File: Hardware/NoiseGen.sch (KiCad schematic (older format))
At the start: 25 parts, among them J1 CONN_01X02, J2 SMA, Q1 BFR92, SW1 SPST, U1 MAX2650, U2 AP2210, U3 MAX2650

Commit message: Added text to PCB, cleaned up PCB
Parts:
- Q1: footprint TO_SOT_Packages_SMD:SOT-323 -> TO_SOT_Packages_SMD:SOT-23
- RV1: footprint Potentiometers:Potentiometer_Trimmer_Bourns_3214G -> FritzLib:Potentiometer_Trimmer_Bourns_3214G
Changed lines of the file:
@@
 F 0 "Q1" H 3741 5154 50  0000 L CNN
 F 1 "BFR92" H 3741 5245 50  0000 L CNN
-F 2 "TO_SOT_Packages_SMD:SOT-323" H 3750 5125 50  0001 L CIN
+F 2 "TO_SOT_Packages_SMD:SOT-23" H 3750 5125 50  0001 L CIN
 F 3 "" H 3550 5200 50  0001 L CNN
 	1    3550 5200
@@
 F 0 "RV1" H 3580 4054 50  0000 R CNN
 F 1 "1k" H 3580 4145 50  0000 R CNN
-F 2 "Potentiometers:Potentiometer_Trimmer_Bourns_3214G" H 3650 4100 50  0001 C CNN
+F 2 "FritzLib:Potentiometer_Trimmer_Bourns_3214G" H 3650 4100 50  0001 C CNN
 F 3 "" H 3650 4100 50  0001 C CNN
 	1    3650 4100

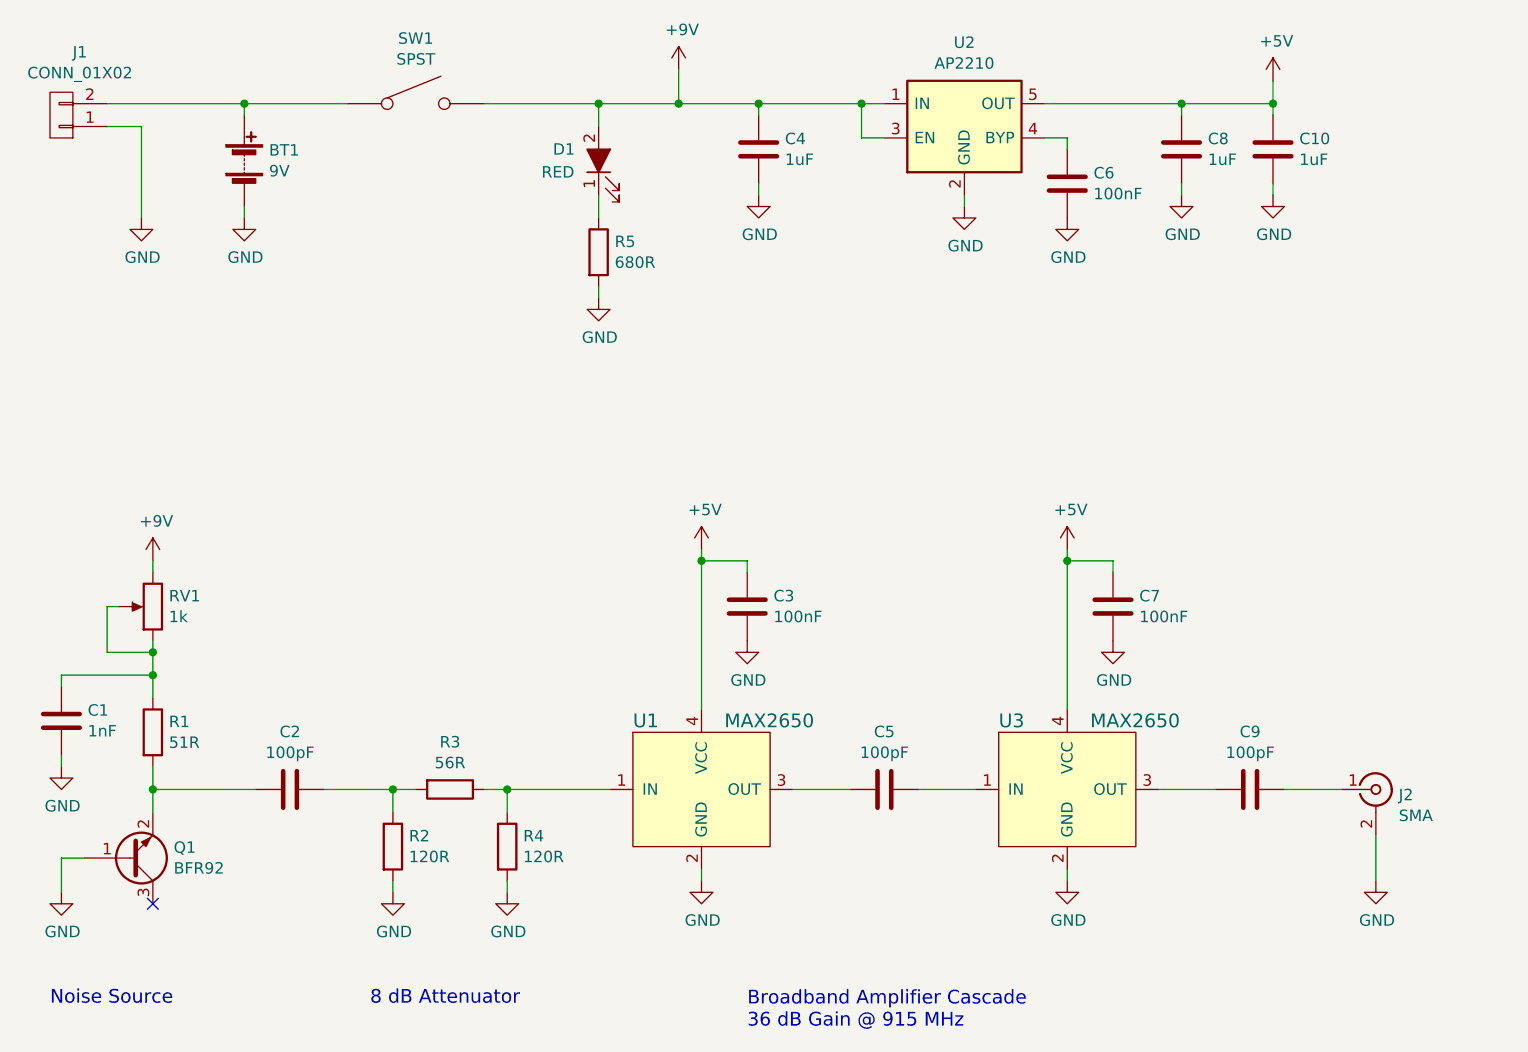
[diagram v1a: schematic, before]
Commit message: Add TVS diode
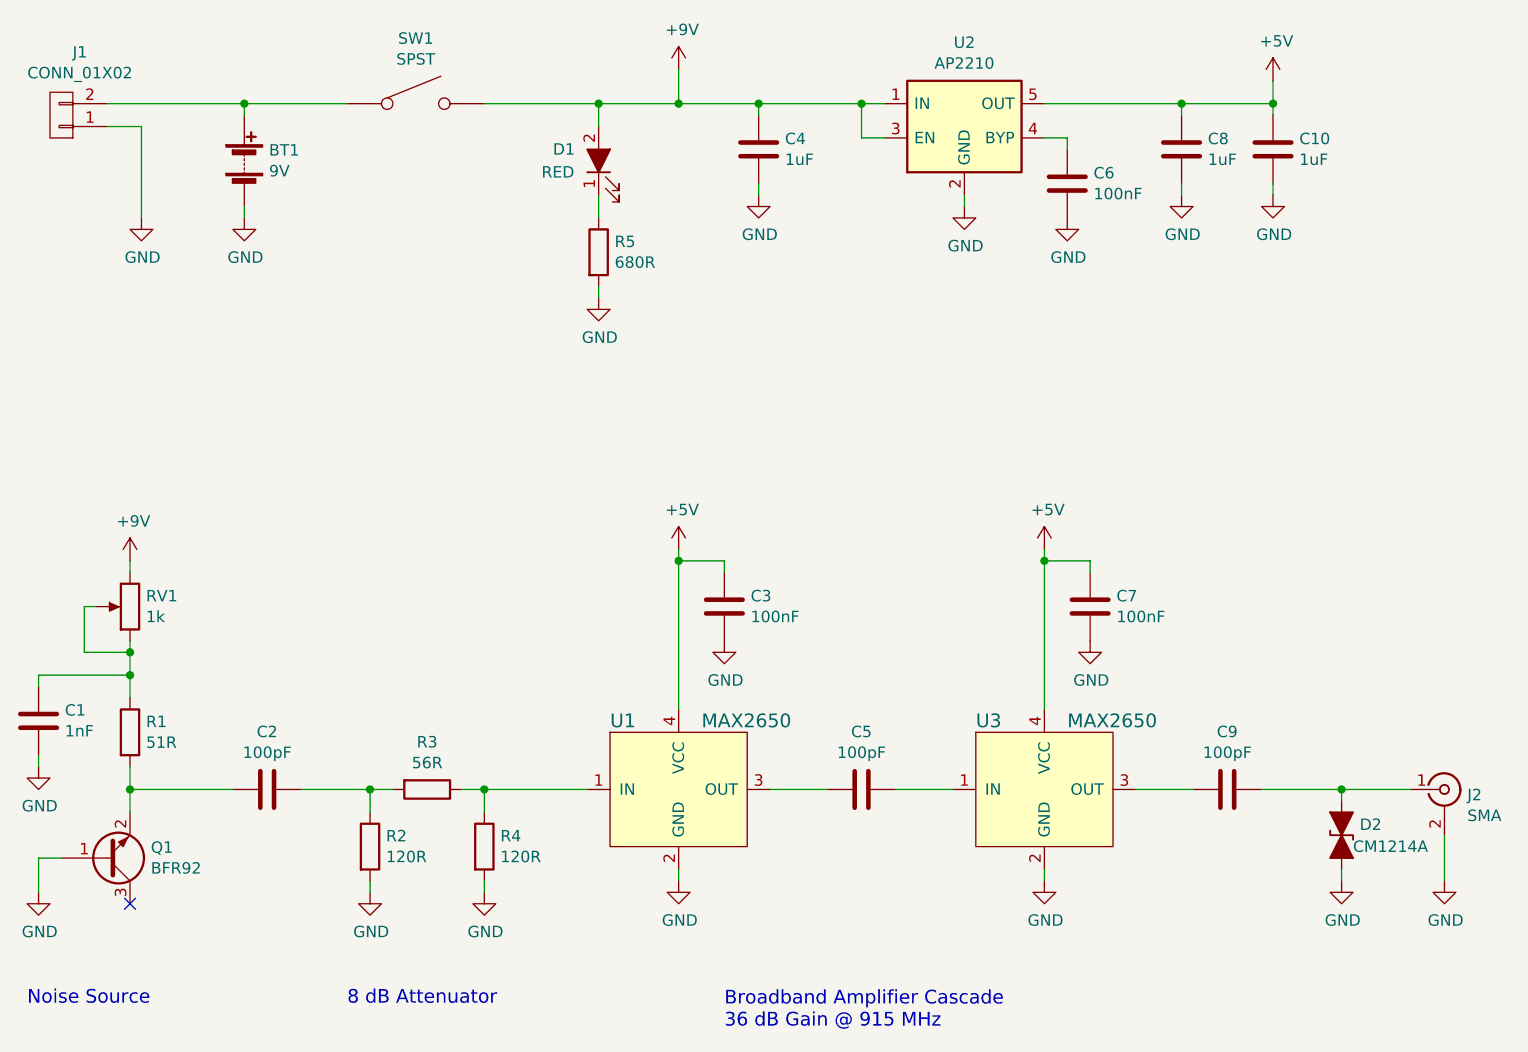
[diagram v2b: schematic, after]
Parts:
- added D2: CM1214A, symbol D_TVS_ALT
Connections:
- net GND: now also D2.2 (A2)
- net at C9.1, J2.1 (In): now also D2.1 (A1)
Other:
- moved on the sheet: C1, C2, C3, C5, C7, C9, J2, Q1, R1, R2, R3, R4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

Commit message: Updated schematic
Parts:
- D2: footprint (none) -> TO_SOT_Packages_SMD:SOT-23
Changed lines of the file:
@@
 $EndComp
 $Comp
-L GND #PWR11
+L GND #PWR01
 U 1 1 598DF451
 P 5950 5300
-F 0 "#PWR11" H 5950 5050 50  0001 C CNN
+F 0 "#PWR01" H 5950 5050 50  0001 C CNN
 F 1 "GND" H 5955 5127 50  0000 C CNN
 F 2 "" H 5950 5300 50  0001 C CNN
@@
 $EndComp
 $Comp
-L GND #PWR16
+L GND #PWR02
 U 1 1 598DF4C0
 P 7550 5300
-F 0 "#PWR16" H 7550 5050 50  0001 C CNN
+F 0 "#PWR02" H 7550 5050 50  0001 C CNN
 F 1 "GND" H 7555 5127 50  0000 C CNN
 F 2 "" H 7550 5300 50  0001 C CNN
@@
 $EndComp
 $Comp
-L +5V #PWR10
+L +5V #PWR03
 U 1 1 598DF579
 P 5950 3850
-F 0 "#PWR10" H 5950 3700 50  0001 C CNN
+F 0 "#PWR03" H 5950 3700 50  0001 C CNN
 F 1 "+5V" H 5965 4023 50  0000 C CNN
 F 2 "" H 5950 3850 50  0001 C CNN
@@
 $EndComp
 $Comp
-L GND #PWR12
+L GND #PWR04
 U 1 1 598DF674
 P 6150 4250
-F 0 "#PWR12" H 6150 4000 50  0001 C CNN
+F 0 "#PWR04" H 6150 4000 50  0001 C CNN
 F 1 "GND" H 6155 4077 50  0000 C CNN
 F 2 "" H 6150 4250 50  0001 C CNN
@@
 $EndComp
 $Comp
-L +5V #PWR15
+L +5V #PWR05
 U 1 1 598DF728
 P 7550 3850
-F 0 "#PWR15" H 7550 3700 50  0001 C CNN
+F 0 "#PWR05" H 7550 3700 50  0001 C CNN
 F 1 "+5V" H 7565 4023 50  0000 C CNN
 F 2 "" H 7550 3850 50  0001 C CNN
@@
 $EndComp
 $Comp
-L GND #PWR18
+L GND #PWR06
 U 1 1 598DF735
 P 7750 4250
-F 0 "#PWR18" H 7750 4000 50  0001 C CNN
+F 0 "#PWR06" H 7750 4000 50  0001 C CNN
 F 1 "GND" H 7755 4077 50  0000 C CNN
 F 2 "" H 7750 4250 50  0001 C CNN
@@
 $EndComp
 $Comp
-L GND #PWR23
+L GND #PWR07
 U 1 1 598DFA37
 P 9300 5300
-F 0 "#PWR23" H 9300 5050 50  0001 C CNN
+F 0 "#PWR07" H 9300 5050 50  0001 C CNN
 F 1 "GND" H 9305 5127 50  0000 C CNN
 F 2 "" H 9300 5300 50  0001 C CNN
@@
 $EndComp
 $Comp
-L +9V #PWR3
+L +9V #PWR08
 U 1 1 598A91DF
 P 3550 3900
-F 0 "#PWR3" H 3550 3750 50  0001 C CNN
+F 0 "#PWR08" H 3550 3750 50  0001 C CNN
 F 1 "+9V" H 3565 4073 50  0000 C CNN
 F 2 "" H 3550 3900 50  0001 C CNN
@@
 $EndComp
 $Comp
-L GND #PWR2
+L GND #PWR09
 U 1 1 598BE8DE
 P 3150 5350
-F 0 "#PWR2" H 3150 5100 50  0001 C CNN
+F 0 "#PWR09" H 3150 5100 50  0001 C CNN
 F 1 "GND" H 3155 5177 50  0000 C CNN
 F 2 "" H 3150 5350 50  0001 C CNN
@@
 $EndComp
 $Comp
-L GND #PWR1
+L GND #PWR010
 U 1 1 598BF110
 P 3150 4800
-F 0 "#PWR1" H 3150 4550 50  0001 C CNN
+F 0 "#PWR010" H 3150 4550 50  0001 C CNN
 F 1 "GND" H 3155 4627 50  0000 C CNN
 F 2 "" H 3150 4800 50  0001 C CNN
@@
 $EndComp
 $Comp
-L GND #PWR6
+L GND #PWR011
 U 1 1 598BF6AF
 P 4600 5350
-F 0 "#PWR6" H 4600 5100 50  0001 C CNN
+F 0 "#PWR011" H 4600 5100 50  0001 C CNN
 F 1 "GND" H 4605 5177 50  0000 C CNN
 F 2 "" H 4600 5350 50  0001 C CNN
@@
 $EndComp
 $Comp
-L GND #PWR7
+L GND #PWR012
 U 1 1 598BF6D8
 P 5100 5350
-F 0 "#PWR7" H 5100 5100 50  0001 C CNN
+F 0 "#PWR012" H 5100 5100 50  0001 C CNN
 F 1 "GND" H 5105 5177 50  0000 C CNN
 F 2 "" H 5100 5350 50  0001 C CNN
@@
 $EndComp
 $Comp
-L +9V #PWR9
+L +9V #PWR013
 U 1 1 598C4FDE
 P 5950 1750
-F 0 "#PWR9" H 5950 1600 50  0001 C CNN
+F 0 "#PWR013" H 5950 1600 50  0001 C CNN
 F 1 "+9V" H 5965 1923 50  0000 C CNN
 F 2 "" H 5950 1750 50  0001 C CNN
@@
 $EndComp
 $Comp
-L GND #PWR13
+L GND #PWR014
 U 1 1 598C578F
 P 6300 2300
-F 0 "#PWR13" H 6300 2050 50  0001 C CNN
+F 0 "#PWR014" H 6300 2050 50  0001 C CNN
 F 1 "GND" H 6305 2127 50  0000 C CNN
 F 2 "" H 6300 2300 50  0001 C CNN
@@
 Connection ~ 5950 1900
 $Comp
-L +5V #PWR20
+L +5V #PWR015
 U 1 1 598C9527
 P 8550 1800
-F 0 "#PWR20" H 8550 1650 50  0001 C CNN
+F 0 "#PWR015" H 8550 1650 50  0001 C CNN
 F 1 "+5V" H 8565 1973 50  0000 C CNN
 F 2 "" H 8550 1800 50  0001 C CNN
@@
 	4050 1900 4050 1950
 $Comp
-L GND #PWR5
+L GND #PWR016
 U 1 1 598D7079
 P 4050 2400
-F 0 "#PWR5" H 4050 2150 50  0001 C CNN
+F 0 "#PWR016" H 4050 2150 50  0001 C CNN
 F 1 "GND" H 4055 2227 50  0000 C CNN
 F 2 "" H 4050 2400 50  0001 C CNN
@@
 Connection ~ 5600 1900
 $Comp
-L GND #PWR8
+L GND #PWR017
 U 1 1 598DE7C4
 P 5600 2750
-F 0 "#PWR8" H 5600 2500 50  0001 C CNN
+F 0 "#PWR017" H 5600 2500 50  0001 C CNN
 F 1 "GND" H 5605 2577 50  0000 C CNN
 F 2 "" H 5600 2750 50  0001 C CNN
@@
 $EndComp
 $Comp
-L GND #PWR19
+L GND #PWR018
 U 1 1 598D4DBB
 P 8150 2300
-F 0 "#PWR19" H 8150 2050 50  0001 C CNN
+F 0 "#PWR018" H 8150 2050 50  0001 C CNN
 F 1 "GND" H 8155 2127 50  0000 C CNN
 F 2 "" H 8150 2300 50  0001 C CNN
@@
 	8550 1800 8550 1950
 $Comp
-L GND #PWR14
+L GND #PWR019
 U 1 1 598D4E8F
 P 7200 2350
-F 0 "#PWR14" H 7200 2100 50  0001 C CNN
+F 0 "#PWR019" H 7200 2100 50  0001 C CNN
 F 1 "GND" H 7205 2177 50  0000 C CNN
 F 2 "" H 7200 2350 50  0001 C CNN
@@
 Connection ~ 8550 1900
 $Comp
-L GND #PWR21
+L GND #PWR020
 U 1 1 598D7087
 P 8550 2300
-F 0 "#PWR21" H 8550 2050 50  0001 C CNN
+F 0 "#PWR020" H 8550 2050 50  0001 C CNN
 F 1 "GND" H 8555 2127 50  0000 C CNN
 F 2 "" H 8550 2300 50  0001 C CNN
@@
 $EndComp
 $Comp
-L GND #PWR17
+L GND #PWR021
 U 1 1 598D79CC
 P 7650 2400
-F 0 "#PWR17" H 7650 2150 50  0001 C CNN
+F 0 "#PWR021" H 7650 2150 50  0001 C CNN
 F 1 "GND" H 7655 2227 50  0000 C CNN
 F 2 "" H 7650 2400 50  0001 C CNN
@@
 $EndComp
 $Comp
-L GND #PWR4
+L GND #PWR022
 U 1 1 5990F7E6
 P 3600 2400
-F 0 "#PWR4" H 3600 2150 50  0001 C CNN
+F 0 "#PWR022" H 3600 2150 50  0001 C CNN
 F 1 "GND" H 3605 2227 50  0000 C CNN
 F 2 "" H 3600 2400 50  0001 C CNN
@@
 F 0 "D2" V 8804 5179 50  0000 L CNN
 F 1 "CM1214A" V 8900 5150 50  0000 L CNN
-F 2 "" H 8850 5100 50  0001 C CNN
+F 2 "TO_SOT_Packages_SMD:SOT-23" H 8850 5100 50  0001 C CNN
 F 3 "" H 8850 5100 50  0001 C CNN
 	1    8850 5100
@@
 $EndComp
 $Comp
-L GND #PWR22
+L GND #PWR023
 U 1 1 59911DC4
 P 8850 5300
-F 0 "#PWR22" H 8850 5050 50  0001 C CNN
+F 0 "#PWR023" H 8850 5050 50  0001 C CNN
 F 1 "GND" H 8855 5127 50  0000 C CNN
 F 2 "" H 8850 5300 50  0001 C CNN
